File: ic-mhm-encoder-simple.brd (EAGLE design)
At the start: 68 x 58.3 mm, 35 parts, among them IC1 LS7183-SOIC, J1 2023960907, J2 2023960607, M1 BSS670S2LH6327XTSA1, SW1 CS-4-13NTA, U1 24LC16BT-I/MC, U2 D5V0F4U6S-7, U3 D5V0F4U6S-7, U4 D5V0F4U6S-7

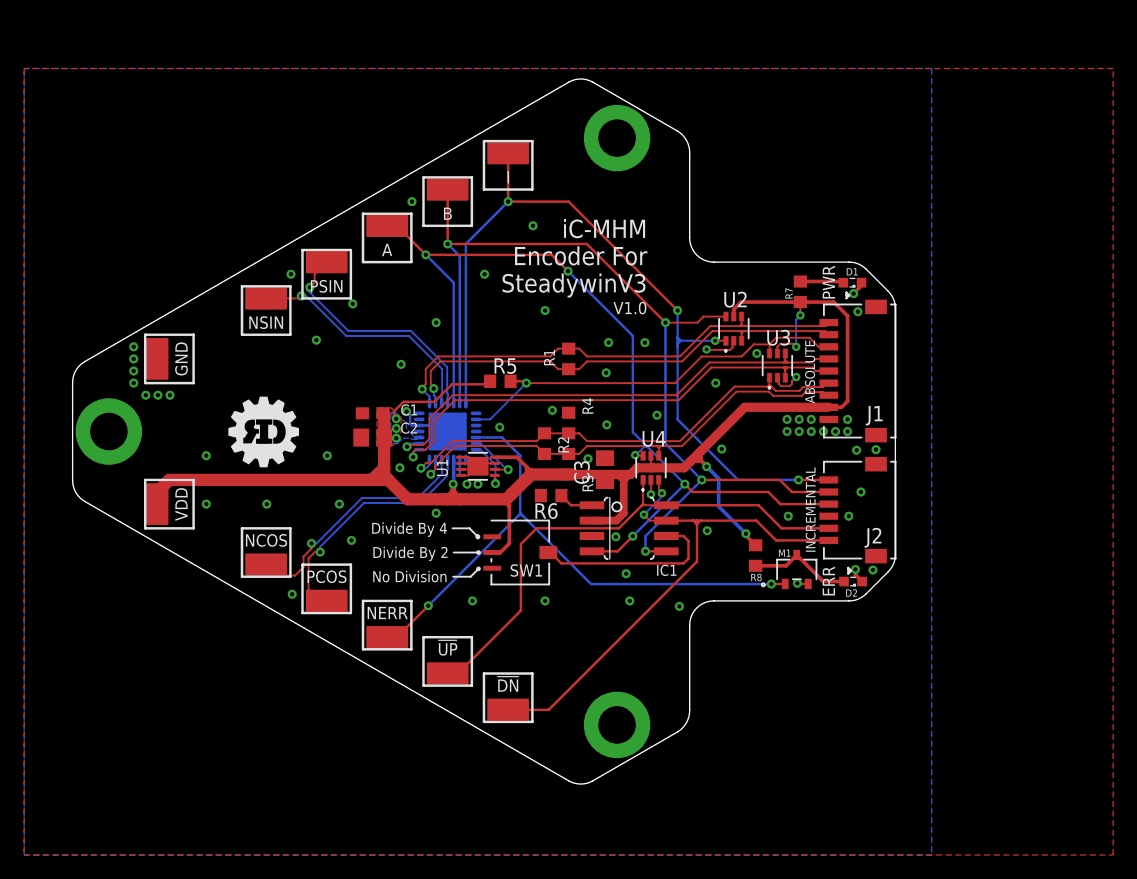
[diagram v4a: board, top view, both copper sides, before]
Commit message: moved termination resistors closer to mhm
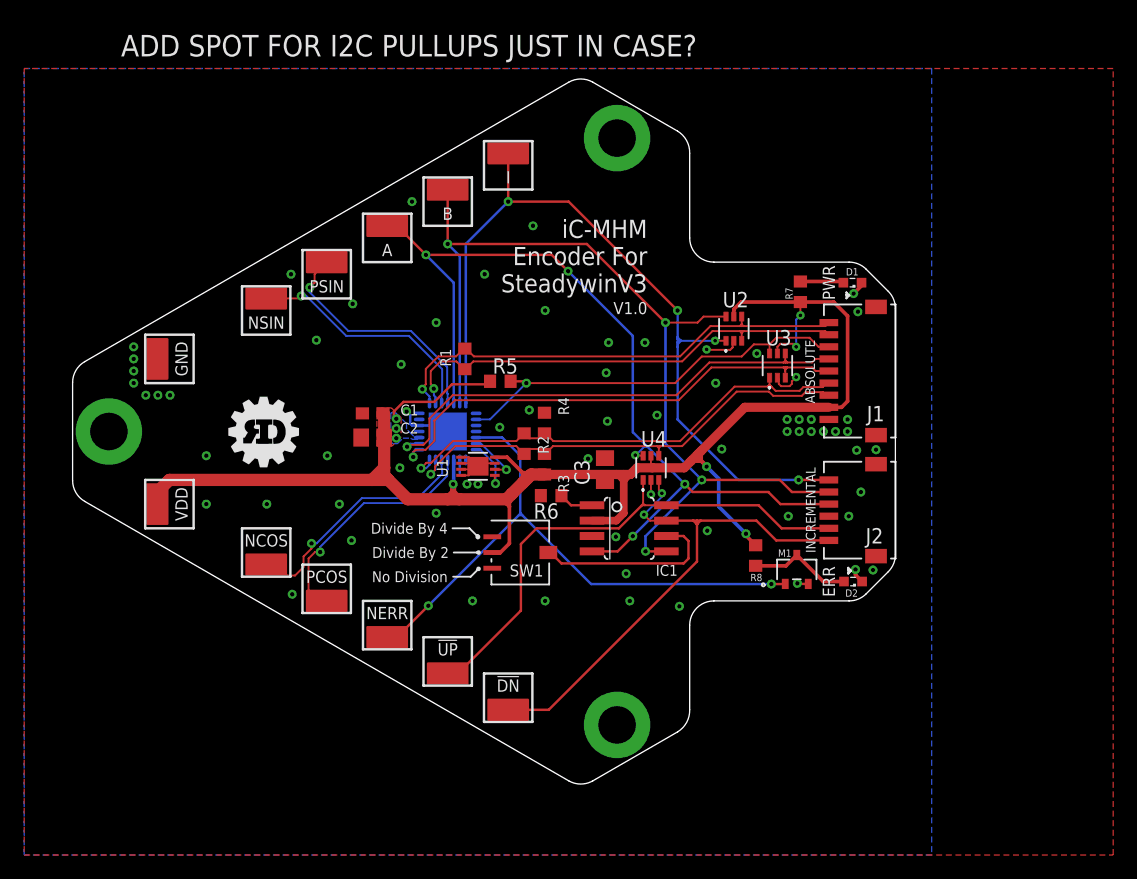
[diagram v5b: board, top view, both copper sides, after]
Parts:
- moved R1 8.58 mm to (1.42, 6.00)
- moved R3 2.00 mm to (8.00, -2.70)
- moved R4 2.00 mm to (8.00, 0.70)
- moved R2 1.69 mm to (6.31, -1.00)
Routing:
- net VDD: track 140.4 -> 142.3 mm
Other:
- board text added: "ADD SPOT FOR I2C PULLUPS JUST IN CASE?"
